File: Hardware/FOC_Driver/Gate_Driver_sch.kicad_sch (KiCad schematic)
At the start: 7 parts, among them IC1 DRV8323RHRGZR

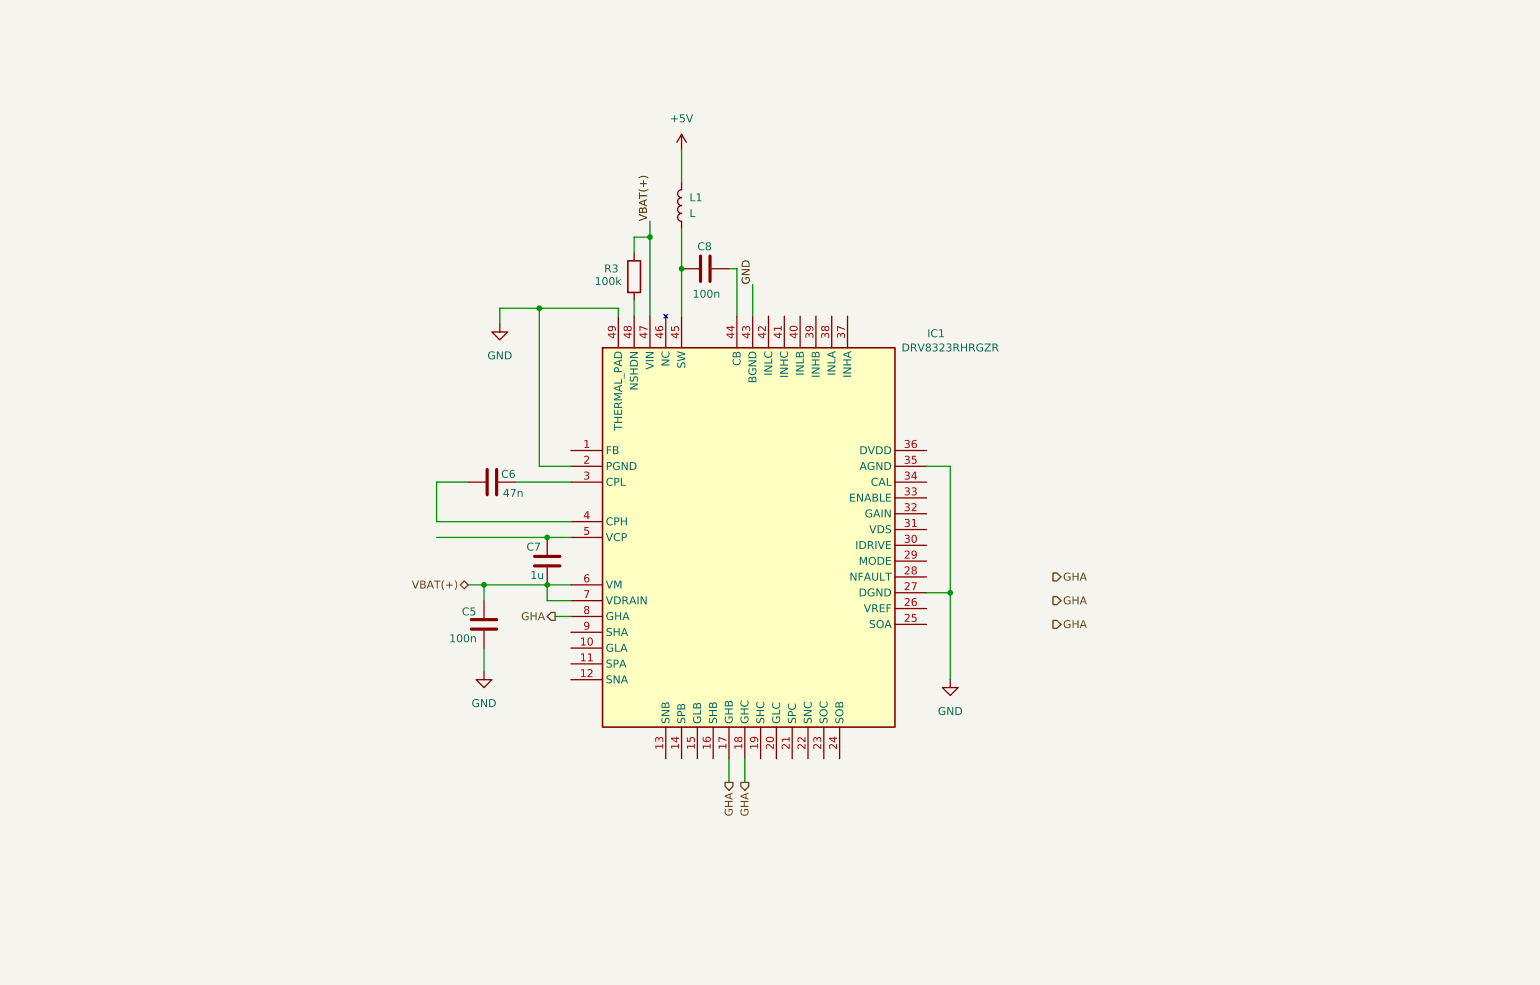
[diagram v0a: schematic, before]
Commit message: Use shared Kicad_Libs instead of project-specific libraries
- Project parts moved to Kicad_Libs (symbol, footprint, 3D, datasheet)
- Lib tables point to ${KIPRJMOD}/../KiCad_Libs (link via bring_libs.bat)
- Schematic/PCB references (lib ids, footprints, 3D paths, datasheets)
  updated to the Kicad_Libs libraries; no design changes
- Removed the old project-specific library folder
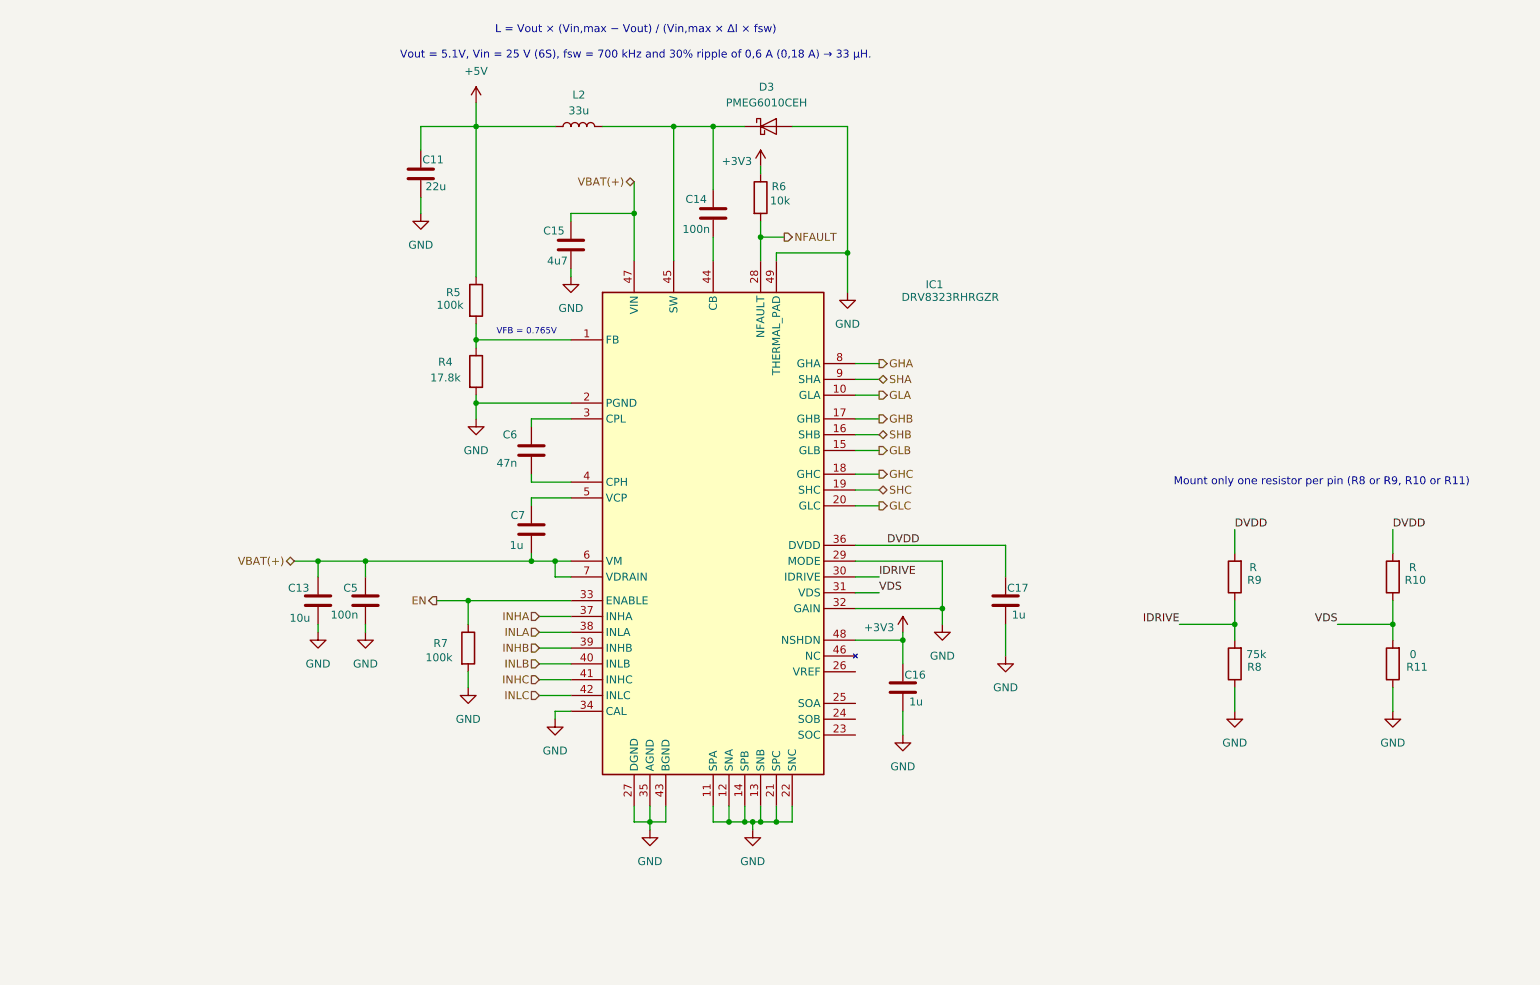
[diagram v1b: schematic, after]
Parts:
- removed C8: 100n, symbol Device:C
- removed L1: L, symbol Device:L
- removed R3: 100k, symbol Device:R
- added C11: 22u, symbol Device:C
- added C13: 10u, symbol Device:C
- added C14: 100n, symbol Device:C
- added C15: 4u7, symbol Device:C
- added C16, C17: 1u, symbol Device:C
- added D3: PMEG6010CEH, Diode_SMD:D_SOD-123F, symbol Diode:PMEG6010CEH
- added L2: 33u, symbol Device:L
- added R10, R9: R, symbol Device:R
- added R11: 0, symbol Device:R
- added R4: 17.8k, symbol Device:R
- added R5, R7: 100k, symbol Device:R
- added R6: 10k, symbol Device:R
- added R8: 75k, symbol Device:R
- IC1: footprint DRV8323RHRGZR:QFN50P700X700X100-49N-D -> eInterface:QFN50P700X700X100-49N-D; symbol DRV8323RHRGZR:DRV8323RHRGZR -> eInterface:DRV8323RHRGZR
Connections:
- net +5V: now also C11.1, L2.1, R5.1
- net GHA: no longer IC1.17 (GHB), IC1.18 (GHC)
- net GND: now also IC1.11 (SPA), IC1.12 (SNA), IC1.13 (SNB), IC1.14 (SPB), IC1.21 (SPC), IC1.22 (SNC), IC1.29 (MODE), IC1.32 (GAIN), IC1.34 (CAL), C11.2, C13.2, C15.1, C16.2, C17.2, D3.2 (A), R11.1, R4.2, R7.2, R8.1
- net VBAT(+): now also C13.1, C15.2
- net at IC1.45 (SW): now also C14.2, D3.1 (K), L2.2
- net at IC1.44 (CB): now also C14.1
- net at IC1.1 (FB): now also R4.1, R5.2
- net GLA: now reaches IC1.10 (GLA)
- net GLB: now reaches IC1.15 (GLB)
- net SHB: now reaches IC1.16 (SHB)
- net SHC: now reaches IC1.19 (SHC)
- net GLC: now reaches IC1.20 (GLC)
- net NFAULT: now reaches IC1.28 (NFAULT)
- net NFAULT: now also R6.2
- net IDRIVE: now reaches IC1.30 (IDRIVE)
- net IDRIVE: now also R8.2, R9.1
- net VDS: now reaches IC1.31 (VDS)
- net VDS: now also R10.1, R11.2
- net EN: now reaches IC1.33 (ENABLE)
- net EN: now also R7.1
- net DVDD: now reaches IC1.36 (DVDD)
- net DVDD: now also C17.1, R10.2, R9.2
- net INHA: now reaches IC1.37 (INHA)
- net INLA: now reaches IC1.38 (INLA)
- net INHB: now reaches IC1.39 (INHB)
- net INLB: now reaches IC1.40 (INLB)
- net INHC: now reaches IC1.41 (INHC)
- net INLC: now reaches IC1.42 (INLC)
- net +3V3: now reaches IC1.48 (NSHDN)
- net +3V3: now also C16.1, R6.1
- net SHA: now reaches IC1.9 (SHA)
- new net GHB: IC1.17 (GHB)
- new net GHC: IC1.18 (GHC)
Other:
- note added: "L = Vout × (Vin,max − Vout) / (Vin,max × ΔI × fsw) Vout = 5.1V, Vin = 25 V (6S), fsw = 700 kHz and 30% ripple of 0,6 A (0,18 A) → 33 µH."
- note added: "Mount only one resistor per pin (R8 or R9, R10 or R11)"
- note added: "VFB = 0.765V"
- moved on the sheet: IC1

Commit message: schematic updates
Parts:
- added R12: R, symbol Device:R
- added R13: 47k, symbol Device:R
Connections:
- net +3V3: now also IC1.26 (VREF); no longer IC1.48 (NSHDN)
- net DVDD: now also R12.2
- net GND: now also R13.1; no longer IC1.11 (SPA), IC1.12 (SNA), IC1.13 (SNB), IC1.14 (SPB), IC1.21 (SPC), IC1.22 (SNC), IC1.32 (GAIN)
- net ISENSE_C: now reaches IC1.23 (SOC)
- net ISENSE_B: now reaches IC1.24 (SOB)
- net ISENSE_A: now reaches IC1.25 (SOA)
- new net GAIN: IC1.32 (GAIN), R12.1, R13.2
- new net SNA: IC1.12 (SNA)
- new net SNB: IC1.13 (SNB)
- new net SNC: IC1.22 (SNC)
- new net SPA: IC1.11 (SPA)
- new net SPB: IC1.14 (SPB)
- new net SPC: IC1.21 (SPC)
- no-connect marks 0 -> 1
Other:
- note added: "GAIN x10"
- note added: "Mount only one resistor per pin (R8 or R9, R10 or R11) R12 not mounted"
- note removed: "Mount only one resistor per pin (R8 or R9, R10 or R11)"
- moved on the sheet: C11, C13, C14, C15, C17, C5, C6, C7, D3, IC1, L2, R10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

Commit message: Schematic update and Firmware folder
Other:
- note added: "IDRIVE_N"
- note added: "IDRIVE_P"
- note added: "VDS"
- note added: "[V]"
- note added: "[mA]"
- moved on the sheet: C11, C13, C14, C15, C16, C17, C5, C6, C7, D3, IC1, L2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

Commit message: schematic completed
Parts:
- added R28: 100k, eResistor:0402, symbol Device:R
- C11, C15: footprint (none) -> eCapacitor:1206
- C13: footprint (none) -> eCapacitor:1210
- C14, C16, C17: footprint (none) -> eCapacitor:0402
- C5, C6, C7: footprint (none) -> eCapacitor:0603
- L2: footprint (none) -> Inductor_SMD:L_Bourns_SRN6045TA
- R10, R12, R9: now not fitted
- R13, R8: footprint (none) -> eResistor:0603
- R4, R5, R6, R7: footprint (none) -> eResistor:0402
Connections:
- net +3V3: now also R28.2
- net at IC1.48 (NSHDN): now also R28.1
- no-connect marks 1 -> 0
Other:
- note added: "3.3V, 30mA"

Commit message: Schematic update, XT30/MR30 connectors and PCB layout in progress
- Connectors: AMASS XT30PW and MR30PW from Kicad_Libs (eConnector)
- Schematic updates on main, MCU and gate driver sheets
- PCB: footprints placed, routing in progress
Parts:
- C15: footprint eCapacitor:1206 -> eCapacitor:0805
- R11: footprint (none) -> eResistor:0603
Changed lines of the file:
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@@
 			)
 		)
-		(property "Footprint" "eCapacitor:1206"
+		(property "Footprint" "eCapacitor:0805"
 			(at 82.8548 71.12 0)
 			(hide yes)
@@
 			)
 		)
-		(property "Footprint" ""
+		(property "Footprint" "eResistor:0603"
 			(at 235.458 138.43 90)
 			(hide yes)

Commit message: Add DNP spare pads for R9, R10, R12 (0603)
- Gate driver: R9, R10, R12 get eResistor:0603 footprint, kept DNP
- PCB: spare 0603 pads placed, excluded from BOM and assembly
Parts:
- R10, R12, R9: footprint (none) -> eResistor:0603
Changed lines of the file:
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@@
 			)
 		)
-		(property "Footprint" ""
+		(property "Footprint" "eResistor:0603"
 			(at 255.778 124.46 90)
 			(hide yes)
@@
 			)
 		)
-		(property "Footprint" ""
+		(property "Footprint" "eResistor:0603"
 			(at 215.138 124.46 90)
 			(hide yes)
@@
 			)
 		)
-		(property "Footprint" ""
+		(property "Footprint" "eResistor:0603"
 			(at 235.458 124.46 90)
 			(hide yes)

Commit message: Finished positioning and started layout v2
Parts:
- R10, R11, R12, R13, R8, R9: footprint eResistor:0603 -> eResistor:0402
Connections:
- net +3V3: no longer R28.2
- net VBAT(+): now also R28.2
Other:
- moved on the sheet: C16
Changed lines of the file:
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@@
 	)
 	(junction
-		(at 153.67 138.43)
-		(diameter 0)
-		(color 0 0 0 0)
-	)
-	(junction
-		(at 153.67 143.51)
+		(at 158.75 143.51)
 		(diameter 0)
 		(color 0 0 0 0)
@@
 	(wire
 		(pts
+			(xy 158.75 151.13) (xy 158.75 157.48)
+		)
+		(stroke
+			(width 0)
+			(type default)
+		)
+	)
+	(wire
+		(pts
 			(xy 77.47 125.73) (xy 81.28 125.73)
 		)
@@
 	(wire
 		(pts
-			(xy 153.67 158.75) (xy 153.67 154.94)
-		)
-		(stroke
-			(width 0)
-			(type default)
-		)
-	)
-	(wire
-		(pts
 			(xy 83.82 128.27) (xy 81.28 128.27)
 		)
@@
 	(wire
 		(pts
-			(xy 140.97 138.43) (xy 153.67 138.43)
-		)
-		(stroke
-			(width 0)
-			(type default)
-		)
-	)
-	(wire
-		(pts
 			(xy 133.35 151.13) (xy 129.54 151.13)
 		)
@@
 	(wire
 		(pts
+			(xy 158.75 139.7) (xy 158.75 143.51)
+		)
+		(stroke
+			(width 0)
+			(type default)
+		)
+	)
+	(wire
+		(pts
 			(xy 116.84 76.2) (xy 128.27 76.2)
 		)
@@
 	(wire
 		(pts
+			(xy 140.97 138.43) (xy 146.05 138.43)
+		)
+		(stroke
+			(width 0)
+			(type default)
+		)
+	)
+	(wire
+		(pts
 			(xy 129.54 93.98) (xy 135.89 93.98)
 		)
@@
 	(wire
 		(pts
-			(xy 153.67 134.62) (xy 153.67 138.43)
-		)
-		(stroke
-			(width 0)
-			(type default)
-		)
-	)
-	(wire
-		(pts
 			(xy 77.47 124.46) (xy 77.47 125.73)
 		)
@@
 	(wire
 		(pts
-			(xy 129.54 143.51) (xy 153.67 143.51)
+			(xy 129.54 143.51) (xy 158.75 143.51)
 		)
 		(stroke
@@
 	(wire
 		(pts
-			(xy 153.67 138.43) (xy 153.67 147.32)
-		)
-		(stroke
-			(width 0)
-			(type default)
-		)
-	)
-	(wire
-		(pts
 			(xy 129.54 125.73) (xy 146.05 125.73)
 		)
@@
 		)
 	)
+	(label "VBAT(+)"
+		(at 146.05 138.43 0)
+		(effects
+			(font
+				(size 1.27 1.27)
+			)
+			(justify left bottom)
+		)
+	)
 	(label "VDS"
 		(at 224.79 132.08 180)
@@
 	(symbol
 		(lib_id "Device:C")
-		(at 153.67 151.13 0)
+		(at 158.75 147.32 0)
 		(unit 1)
 		(body_style 1)
@@
 		(dnp no)
 		(property "Reference" "C16"
-			(at 153.924 149.098 0)
+			(at 159.004 145.288 0)
 			(show_name no)
 			(do_not_autoplace no)
@@
 		)
 		(property "Value" "1u"
-			(at 154.686 153.416 0)
+			(at 159.766 149.606 0)
 			(show_name no)
 			(do_not_autoplace no)
@@
 		)
 		(property "Footprint" "eCapacitor:0402"
-			(at 154.6352 154.94 0)
+			(at 159.7152 151.13 0)
 			(hide yes)
 			(show_name no)
@@
 		)
 		(property "Datasheet" ""
-			(at 153.67 151.13 0)
+			(at 158.75 147.32 0)
 			(hide yes)
 			(show_name no)
@@
 		)
 		(property "Description" "1u,10V"
-			(at 153.67 151.13 0)
+			(at 158.75 147.32 0)
 			(hide yes)
 			(show_name no)
@@
 			)
 		)
-		(property "Footprint" "eResistor:0603"
+		(property "Footprint" "eResistor:0402"
 			(at 255.778 124.46 90)
 			(hide yes)
@@
 			)
 		)
-		(property "Footprint" "eResistor:0603"
+		(property "Footprint" "eResistor:0402"
 			(at 215.138 124.46 90)
 			(hide yes)
@@
 	(symbol
 		(lib_id "power:GND")
-		(at 153.67 158.75 0)
+		(at 158.75 157.48 0)
 		(unit 1)
 		(body_style 1)
@@
 		(fields_autoplaced yes)
 		(property "Reference" "#PWR036"
-			(at 153.67 165.1 0)
+			(at 158.75 163.83 0)
 			(hide yes)
 			(show_name no)
@@
 		)
 		(property "Value" "GND"
-			(at 153.67 163.83 0)
+			(at 158.75 162.56 0)
 			(show_name no)
 			(do_not_autoplace no)
@@
 		)
 		(property "Footprint" ""
-			(at 153.67 158.75 0)
+			(at 158.75 157.48 0)
 			(hide yes)
 			(show_name no)
@@
 		)
 		(property "Datasheet" ""
-			(at 153.67 158.75 0)
+			(at 158.75 157.48 0)
 			(hide yes)
 			(show_name no)
@@
 		)
 		(property "Description" "Power symbol creates a global label with name \"GND\" , ground"
-			(at 153.67 158.75 0)
+			(at 158.75 157.48 0)
 			(hide yes)
 			(show_name no)
@@
 			)
 		)
-		(property "Footprint" "eResistor:0603"
+		(property "Footprint" "eResistor:0402"
 			(at 215.138 138.43 90)
 			(hide yes)
@@
 			)
 		)
-		(property "Footprint" "eResistor:0603"
+		(property "Footprint" "eResistor:0402"
 			(at 235.458 138.43 90)
 			(hide yes)
@@
 			)
 		)
-		(property "Footprint" "eResistor:0603"
+		(property "Footprint" "eResistor:0402"
 			(at 235.458 124.46 90)
 			(hide yes)
@@
 			)
 		)
-		(property "Footprint" "eResistor:0603"
+		(property "Footprint" "eResistor:0402"
 			(at 255.778 138.43 90)
 			(hide yes)
@@
 	)
 	(symbol
-		(lib_id "power:GND")
-		(at 68.58 102.87 0)
+		(lib_id "power:+3V3")
+		(at 158.75 139.7 0)
 		(unit 1)
 		(body_style 1)
@@
 		(in_pos_files yes)
 		(dnp no)
-		(fields_autoplaced yes)
-		(property "Reference" "#PWR031"
-			(at 68.58 109.22 0)
+		(property "Reference" "#PWR037"
+			(at 158.75 143.51 0)
 			(hide yes)
 			(show_name no)
@@
 			)
 		)
-		(property "Value" "GND"
-			(at 68.58 107.95 0)
+		(property "Value" "+3V3"
+			(at 158.242 135.89 0)
 			(show_name no)
 			(do_not_autoplace no)
@@
 		)
 		(property "Footprint" ""
-			(at 68.58 102.87 0)
+			(at 158.75 139.7 0)
 			(hide yes)
 			(show_name no)
@@
 		)
 		(property "Datasheet" ""
-			(at 68.58 102.87 0)
+			(at 158.75 139.7 0)
 			(hide yes)
 			(show_name no)
@@
 			)
 		)
-		(property "Description" "Power symbol creates a global label with name \"GND\" , ground"
-			(at 68.58 102.87 0)
+		(property "Description" "Power symbol creates a global label with name \"+3V3\""
+			(at 158.75 139.7 0)
 			(hide yes)
 			(show_name no)
@@
 			(project "FOC_Driver"
 				(path "/56350f0b-fa2d-4452-8705-62cde497823d/acd2d756-a5c8-49b7-a17f-f63fae77db1e"
-					(reference "#PWR031")
+					(reference "#PWR037")
 					(unit 1)
 				)
@@
 	)
 	(symbol
-		(lib_id "Device:C")
-		(at 77.47 120.65 180)
+		(lib_id "power:GND")
+		(at 68.58 102.87 0)
 		(unit 1)
 		(body_style 1)
@@
 		(in_pos_files yes)
 		(dnp no)
-		(property "Reference" "C7"
-			(at 76.454 118.364 0)
+		(fields_autoplaced yes)
+		(property "Reference" "#PWR031"
+			(at 68.58 109.22 0)
+			(hide yes)
 			(show_name no)
 			(do_not_autoplace no)
@@
 					(size 1.27 1.27)
 				)
-				(justify left)
 			)
 		)
-		(property "Value" "1u"
-			(at 76.2 123.19 0)
+		(property "Value" "GND"
+			(at 68.58 107.95 0)
 			(show_name no)
 			(do_not_autoplace no)
@@
 					(size 1.27 1.27)
 				)
-				(justify left)
 			)
 		)
-		(property "Footprint" "eCapacitor:0603"
-			(at 76.5048 116.84 0)
+		(property "Footprint" ""
+			(at 68.58 102.87 0)
 			(hide yes)
 			(show_name no)
@@
 		)
 		(property "Datasheet" ""
-			(at 77.47 120.65 0)
+			(at 68.58 102.87 0)
 			(hide yes)
 			(show_name no)
@@
 			)
 		)
-		(property "Description" "1u,25V"
-			(at 77.47 120.65 0)
+		(property "Description" "Power symbol creates a global label with name \"GND\" , ground"
+			(at 68.58 102.87 0)
 			(hide yes)
 			(show_name no)
@@
 		(pin "1"
 		)
-		(pin "2"
-		)
 		(instances
 			(project "FOC_Driver"
 				(path "/56350f0b-fa2d-4452-8705-62cde497823d/acd2d756-a5c8-49b7-a17f-f63fae77db1e"
-					(reference "C7")
+					(reference "#PWR031")
 					(unit 1)
 				)
@@
 	)
 	(symbol
-		(lib_id "power:+3V3")
-		(at 153.67 134.62 0)
+		(lib_id "Device:C")
+		(at 77.47 120.65 180)
 		(unit 1)
 		(body_style 1)
@@
 		(in_pos_files yes)
 		(dnp no)
-		(property "Reference" "#PWR037"
-			(at 153.67 138.43 0)
-			(hide yes)
+		(property "Reference" "C7"
+			(at 76.454 118.364 0)
 			(show_name no)
 			(do_not_autoplace no)
@@
 					(size 1.27 1.27)
 				)
+				(justify left)
 			)
 		)
-		(property "Value" "+3V3"
-			(at 153.162 130.81 0)
+		(property "Value" "1u"
+			(at 76.2 123.19 0)
 			(show_name no)
 			(do_not_autoplace no)
@@
 					(size 1.27 1.27)
 				)
+				(justify left)
 			)
 		)
-		(property "Footprint" ""
-			(at 153.67 134.62 0)
+		(property "Footprint" "eCapacitor:0603"
+			(at 76.5048 116.84 0)
 			(hide yes)
 			(show_name no)
@@
 		)
 		(property "Datasheet" ""
-			(at 153.67 134.62 0)
+			(at 77.47 120.65 0)
 			(hide yes)
 			(show_name no)
@@
 			)
 		)
-		(property "Description" "Power symbol creates a global label with name \"+3V3\""
-			(at 153.67 134.62 0)
+		(property "Description" "1u,25V"
+			(at 77.47 120.65 0)
 			(hide yes)
 			(show_name no)
@@
 		(pin "1"
 		)
+		(pin "2"
+		)
 		(instances
 			(project "FOC_Driver"
 				(path "/56350f0b-fa2d-4452-8705-62cde497823d/acd2d756-a5c8-49b7-a17f-f63fae77db1e"
-					(reference "#PWR037")
+					(reference "C7")
 					(unit 1)
 				)
